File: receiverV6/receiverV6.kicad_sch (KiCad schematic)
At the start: 15 parts, among them IC1 AP7361C-33E-13, J2 adafruitpwr1000, J3 S2B-PH-SM4-TB, J4 S2B-PH-SM4-TB, J5 S2B-PH-SM4-TB, J6 MM60-52B1-E1-R650, U1 Teensy4.0

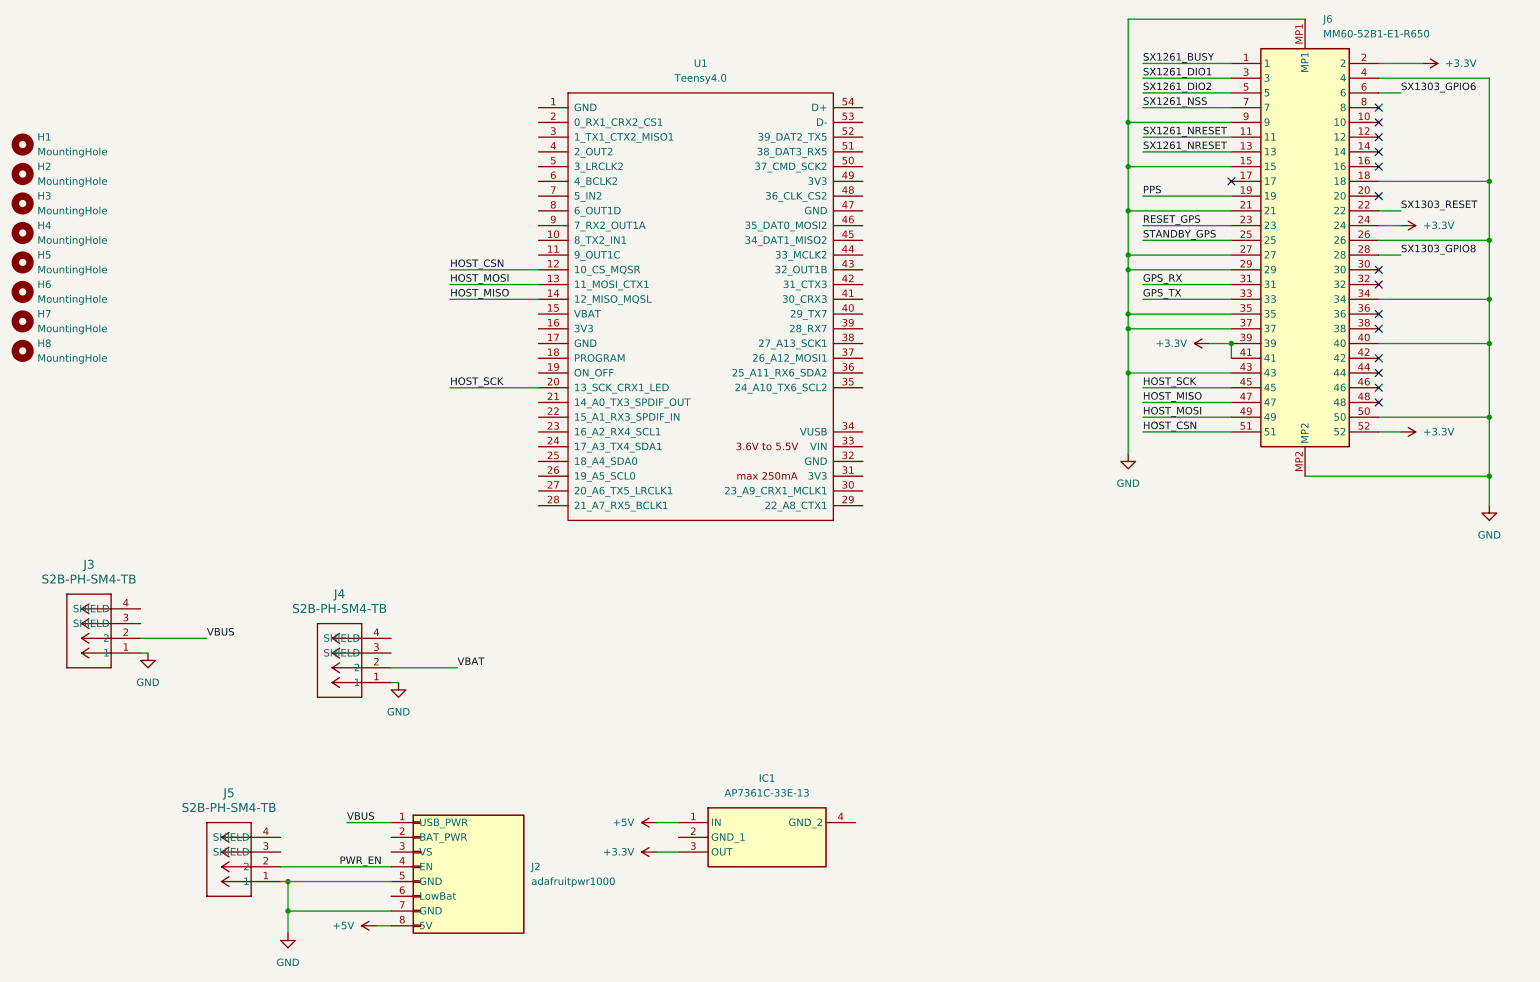
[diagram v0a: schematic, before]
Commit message: add rp2350 design
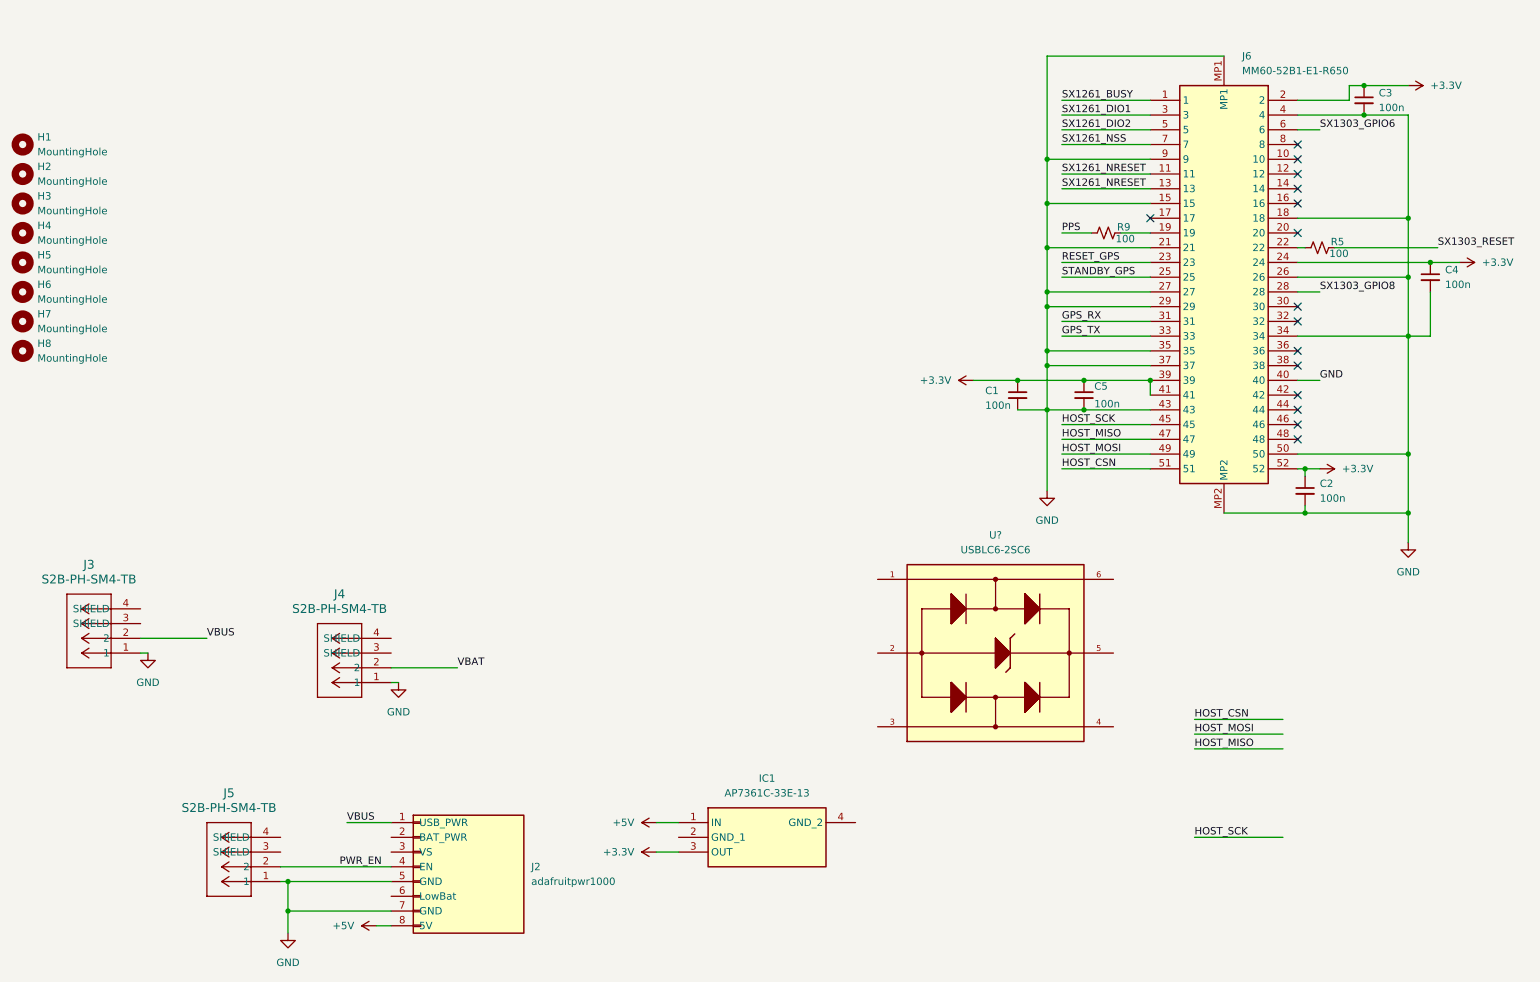
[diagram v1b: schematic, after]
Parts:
- removed U1: Teensy4.0, teensy:Teensy40_smd_mod_receiver, symbol teensy:Teensy4.0
- added C1, C2, C3, C5: 100n, Capacitor_SMD:C_0402_1005Metric, symbol Device:C_Small
- added C4: 100n, symbol Device:C_Small
- added R5, R9: 100, Resistor_SMD:R_0402_1005Metric_Pad0.72x0.64mm_HandSolder, symbol Device:R_Small_US
- added U?: USBLC6-2SC6, USBLC6-2SC6:SOT95P280X145-6N, symbol USBLC6-2SC6:USBLC6-2SC6
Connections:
- net +3.3V: now also C1.1, C2.1, C3.1, C4.1, C5.1
- net GND: now also C1.2, C2.2, C3.2, C4.2, C5.2
- net PPS: now also R9.1; no longer J6.19
- net SX1303_RESET: now also R5.2; no longer J6.22
- new net: J6.22, R5.1
- new net: J6.19, R9.2
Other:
- moved on the sheet: J6
